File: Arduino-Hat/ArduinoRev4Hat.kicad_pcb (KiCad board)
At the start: 2 copper layers, 42.8 x 83.5 mm, 12 parts, among them J1 Conn_01x10_Pin, J10 73099-0, J11 73099-0, J2 Conn_01x08_Pin, J3 Conn_01x04_Pin, J4 Conn_01x04_Pin, J5 Conn_01x04_Pin, J6 73099-0, J7 73099-0, J8 73099-0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

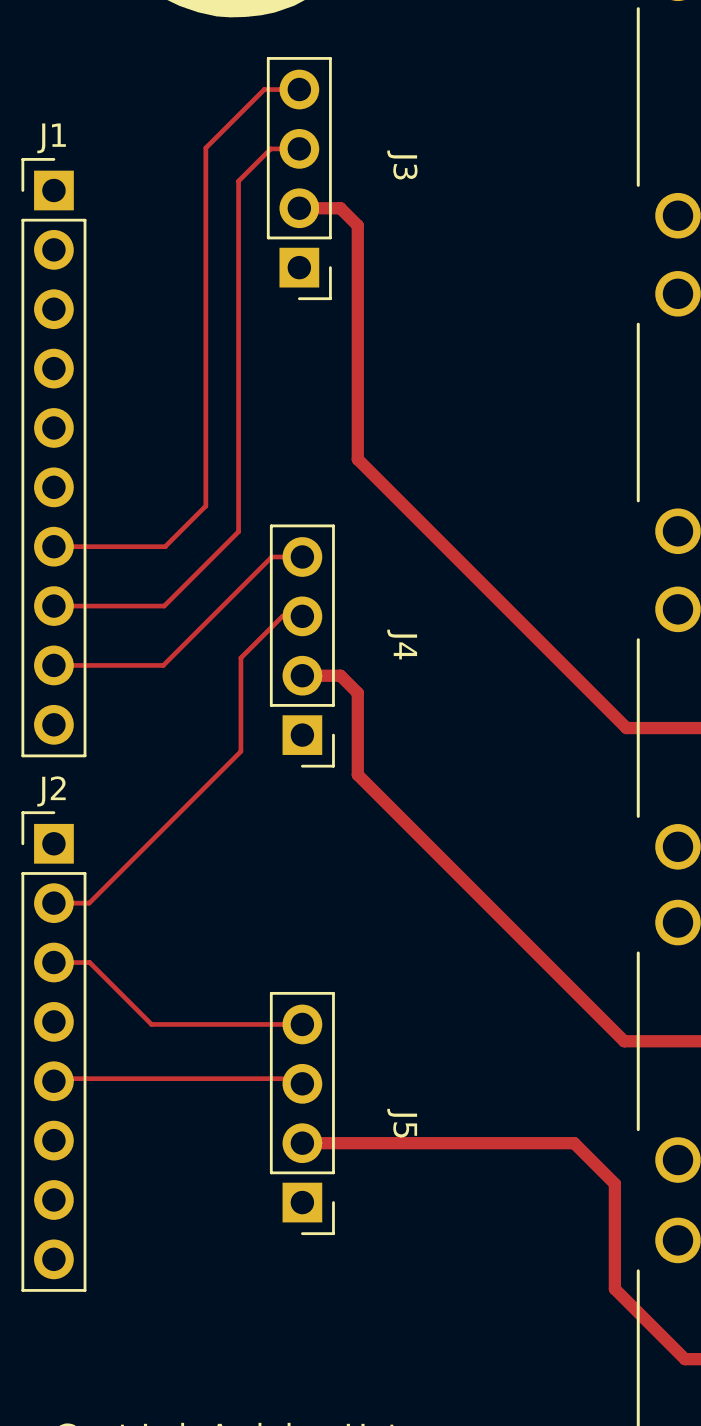
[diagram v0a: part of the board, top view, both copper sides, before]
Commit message: finailzied prototype for the magnetometer pcb
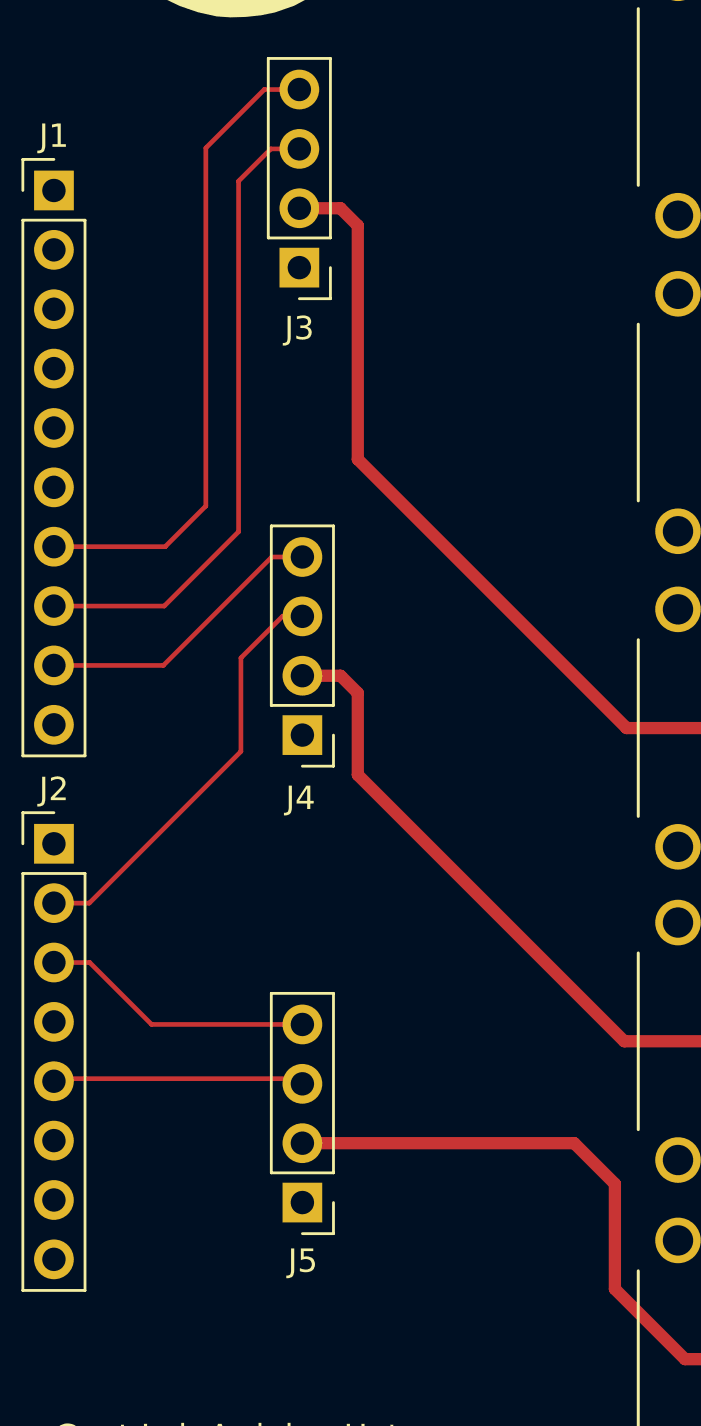
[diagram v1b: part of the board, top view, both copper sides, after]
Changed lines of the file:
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@@
 			(at 1 5 0)
 			(layer "F.Fab")
+			(hide yes)
 			(effects
 				(font
@@
 		(tags "Through hole pin header THT 1x04 2.54mm single row")
 		(property "Reference" "J5"
-			(at -4.37 3.3 -90)
+			(at -0.02 -2.5 0)
 			(unlocked yes)
 			(layer "F.SilkS")
@@
 			(at 3.13 4.3 90)
 			(layer "F.Fab")
+			(hide yes)
 			(effects
 				(font
@@
 			(at 1.25 -5 0)
 			(layer "F.Fab")
+			(hide yes)
 			(effects
 				(font
@@
 			(at 1.25 -5 0)
 			(layer "F.Fab")
+			(hide yes)
 			(effects
 				(font
@@
 		(tags "Through hole pin header THT 1x04 2.54mm single row")
 		(property "Reference" "J4"
-			(at -4.37 3.8 -90)
+			(at 0.08 -2.7 0)
 			(unlocked yes)
 			(layer "F.SilkS")
@@
 			(at 0 9.95 0)
 			(layer "F.Fab")
+			(hide yes)
 			(effects
 				(font
@@
 			(at 1 4.85 0)
 			(layer "F.Fab")
+			(hide yes)
 			(effects
 				(font
@@
 			(at 1.25 -5 0)
 			(layer "F.Fab")
+			(hide yes)
 			(effects
 				(font
@@
 			(at 1.25 5 0)
 			(layer "F.Fab")
+			(hide yes)
 			(effects
 				(font
@@
 			(at 0.508 26.797 0)
 			(layer "F.Fab")
+			(hide yes)
 			(effects
 				(font
@@
 		(tags "Through hole pin header THT 1x04 2.54mm single row")
 		(property "Reference" "J3"
-			(at -4.5 4.3 -90)
+			(at 0 -2.6 0)
 			(unlocked yes)
 			(layer "F.SilkS")
@@
 			(at 0 9.95 0)
 			(layer "F.Fab")
+			(hide yes)
 			(effects
 				(font
@@
 			(at 0 20.11 0)
 			(layer "F.Fab")
+			(hide yes)
 			(effects
 				(font
@@
 		)
 	)
-	(group ""
-		(members "935f2623-a0f9-4c79-871a-c09389eb87c0" "bc6e2576-27ad-42bb-a951-a4d988f9a3fd"
-			"ec0ea479-60b9-422e-8927-8c2edca35275" "f4733074-2fef-4a37-a63b-7e0b9d5c95ae"
-		)
-	)

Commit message: updates pcb for arduino
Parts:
- removed J1: Conn_01x10_Pin, Connector_PinHeader_2.54mm:PinHeader_1x10_P2.54mm_Vertical
- removed J2: Conn_01x08_Pin, Connector_PinHeader_2.54mm:PinHeader_1x08_P2.54mm_Vertical
- added A1: Arduino_Uno_R4_WiFi_Shield, my_custom:Arduino_Uno_R4_WiFi_Shield, F.Cu at (106.2, 40.0)
- moved G*** 101.0 mm to (179.4, 63.6)
- moved J7 95.7 mm to (180.1, 116.8), turned to -90 degrees
- moved J3 87.4 mm to (166.1, 64.0)
- moved J4 87.4 mm to (166.2, 84.0)
- moved J5 87.4 mm to (166.2, 104.0)
- moved J8 77.0 mm to (166.6, 116.8), turned to -90 degrees
- moved J6 58.6 mm to (153.1, 116.8), turned to -90 degrees
- moved J9 40.8 mm to (139.6, 116.8), turned to -90 degrees
- moved J10 25.2 mm to (126.2, 116.8), turned to -90 degrees
- moved J11 18.0 mm to (112.6, 116.8), turned to -90 degrees
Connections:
- J10 pad 1: /VM_Y -> GND
- J11 pad 1: /VM_Z -> GND
- J6 pad 1: GND -> /VM_Z
- J7 pad 1: GND -> /VM_X
- J8 pad 1: GND -> /VM_Y
- J9 pad 1: /VM_X -> GND
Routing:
- net /VM_X: track 35.1 -> 61.4 mm
- net /VM_Y: track 28.4 -> 40.0 mm
- net /IN2_X: track 28.1 -> 21.4 mm
- net /IN1_X: track 27.4 -> 21.5 mm
- net /VM_Z: track 28.8 -> 23.7 mm
- net /IN2_Y: track 12.6 -> 14.3 mm
- net /IN1_Y: track 18.1 -> 16.8 mm
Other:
- board size 42.8 x 83.5 mm -> 84.5 x 71.5 mm

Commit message: newest version
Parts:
- removed the G*** at (179.4, 63.6)
- added G***: LOGO, LOGO, F.Cu at (197.2, 106.7)
- added G***: LOGO, LOGO, F.Cu at (162.5, 132.6)
- moved J9 81.6 mm to (196.2, 47.5), turned to 90 degrees
- moved J6 81.5 mm to (155.4, 47.5), turned to 90 degrees
- moved J11 71.2 mm to (182.7, 47.5), turned to 90 degrees
- moved J8 71.0 mm to (141.8, 47.5), turned to 90 degrees
- moved J7 70.2 mm to (128.4, 47.5), turned to 90 degrees
- moved J10 70.2 mm to (169.2, 47.5), turned to 90 degrees
- moved J3 58.1 mm to (132.4, 111.4), turned to 0 degrees
- moved J5 49.4 mm to (132.3, 68.1), turned to 0 degrees
- moved A1 36.7 mm to (136.3, 60.9)
- moved J4 34.4 mm to (132.3, 89.8), turned to 0 degrees
- renumbered J7 to J10, J8 to J11, J11 to J6, J9 to J7, J10 to J8, J6 to J9
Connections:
- A1 pad GND1: unconnected-(A1-GND-PadGND1) -> GND
- A1 pad GND2: unconnected-(A1-GND-PadGND2) -> GND
- J10 pad 1: /VM_X -> GND
- J11 pad 1: /VM_Y -> GND
- J3 pad 2: /VM_X -> /VM_Z
- J3 pad 3: /IN1_X -> /IN1_Z
- J3 pad 4: /IN2_X -> /IN2_Z
- J5 pad 2: /VM_Z -> /VM_X
- J5 pad 3: /IN1_Z -> /IN1_X
- J5 pad 4: /IN2_Z -> /IN2_X
- J6 pad 1: GND -> /VM_X
- J7 pad 1: GND -> /VM_Z
- J8 pad 1: GND -> /VM_Y
- J9 pad 1: /VM_Z -> GND
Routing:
- net /IN1_X: track 21.5 -> 121.5 mm
- net /IN2_X: track 21.4 -> 117.9 mm
- net /IN2_Y: track 14.3 -> 108.6 mm
- net /IN1_Y: track 16.8 -> 106.5 mm
- net /IN2_Z: track 11.5 -> 89.1 mm
- net /IN1_Z: track 10.6 -> 81.0 mm
- net /VM_Z: track 23.7 -> 70.7 mm
- net /VM_X: track 61.4 -> 43.1 mm
- net /VM_Y: track 40.0 -> 56.2 mm
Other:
- board size 84.5 x 71.5 mm -> 97.7 x 104.1 mm
- board text added: "Andres Perez '28 John Nisbet '27 Bernie Lozano '27 Andrew Collette '26 Tyler Hanson '26"
- board text added: "Helmholtz Driver V2"
- board text removed: "Goat Lab Arduino Hat by Andres Perez (28')"
